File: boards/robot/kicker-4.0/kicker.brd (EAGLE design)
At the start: 141 x 146.1 mm, 158 parts, among them J1 B2PS-VH(LF)(SN), J100 B2PS-VH(LF)(SN), J101 B2PS-VH(LF)(SN), J2 2-PIN_2MM-H, J3 3-PIN_2MM-H, J4 SFW8R-1STE1LF, Q1 BSS127, Q100 AOD1N60, Q101 BSS127, Q2 BSS127, Q3 BSS127, Q4 BSS806NSOT-23-3, Q5 ATP302ATPAK, Q6 IXGK400N30A3, Q7 IXGK400N30A3, Q8 IRFS4227, T1 DA203X-ALDA2034, U1 IX4427N, U100 15V, U2 MPM3620GQV-P, U3 ADUM7441CRQZ-RL7, U4 ADUM7441ARQZ-RL7, U5 AT32ATQFP44, U6 LT3751FE

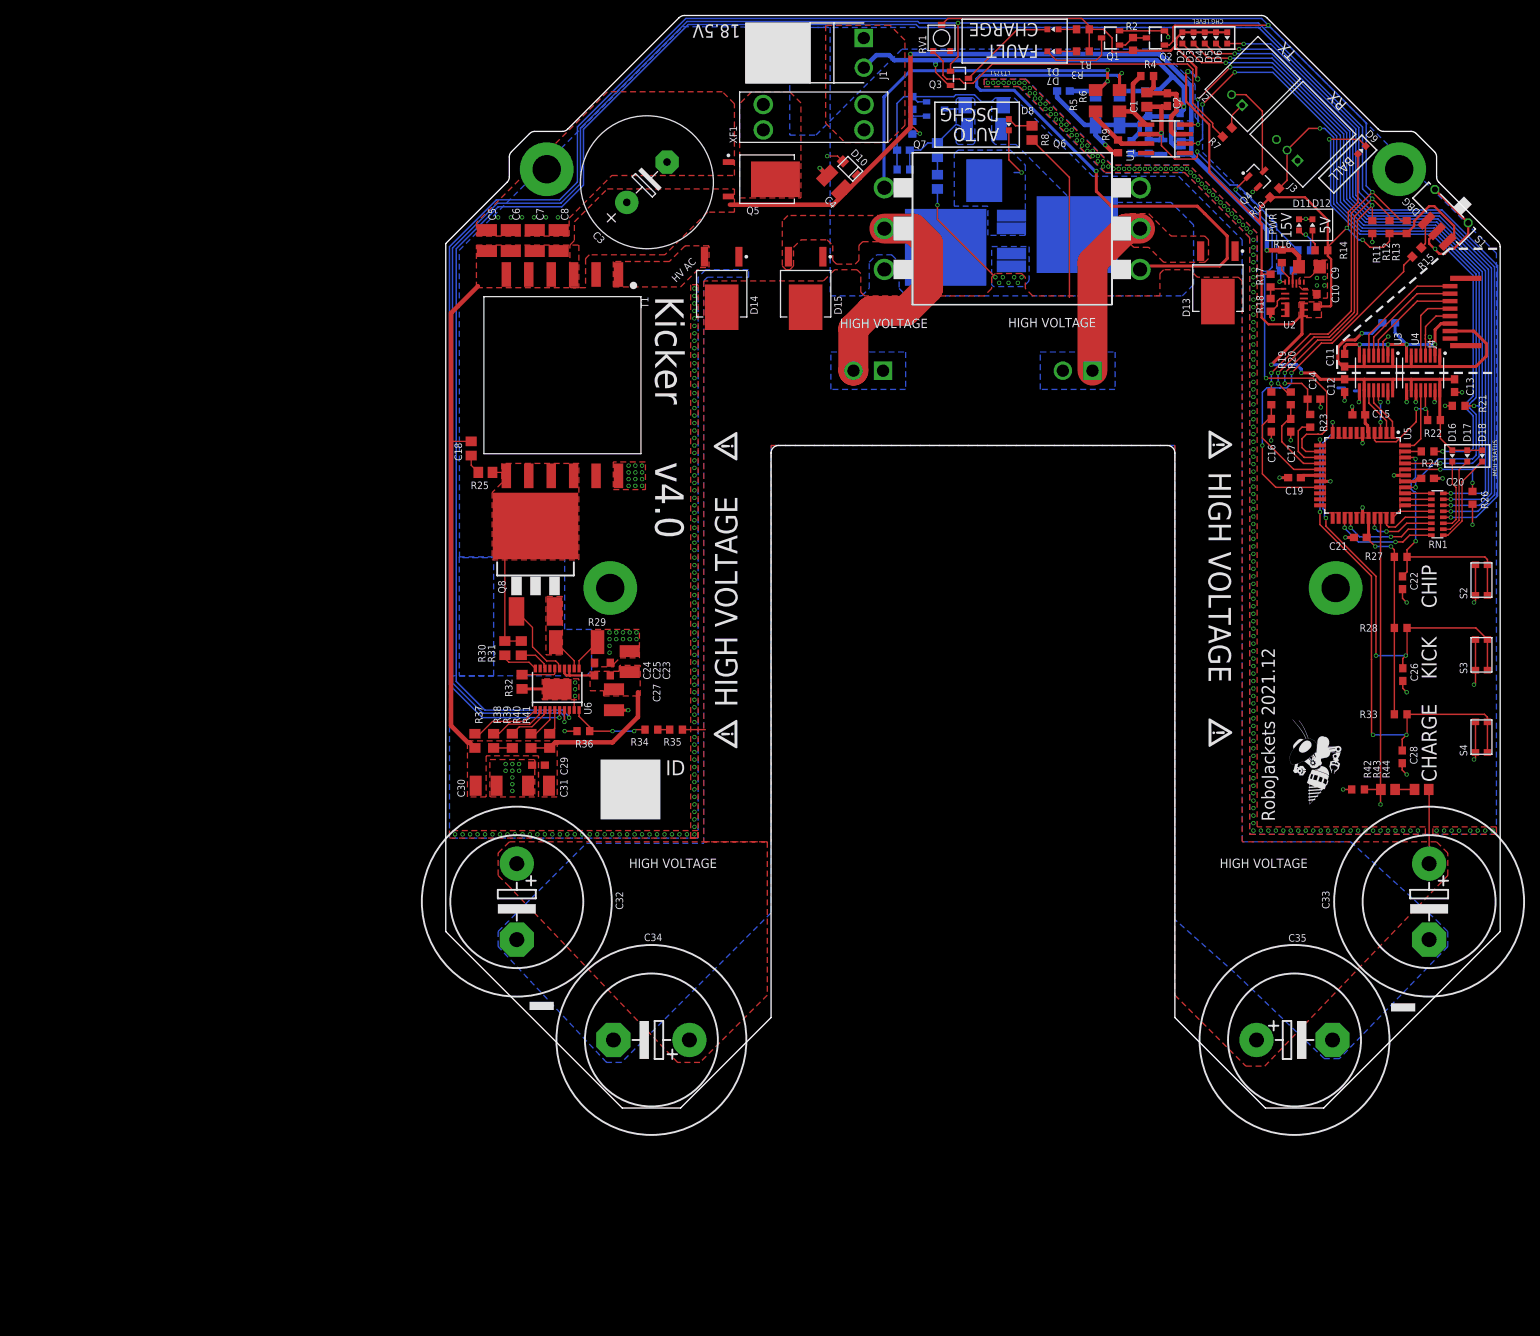
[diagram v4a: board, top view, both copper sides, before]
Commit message: Replaced power connectors
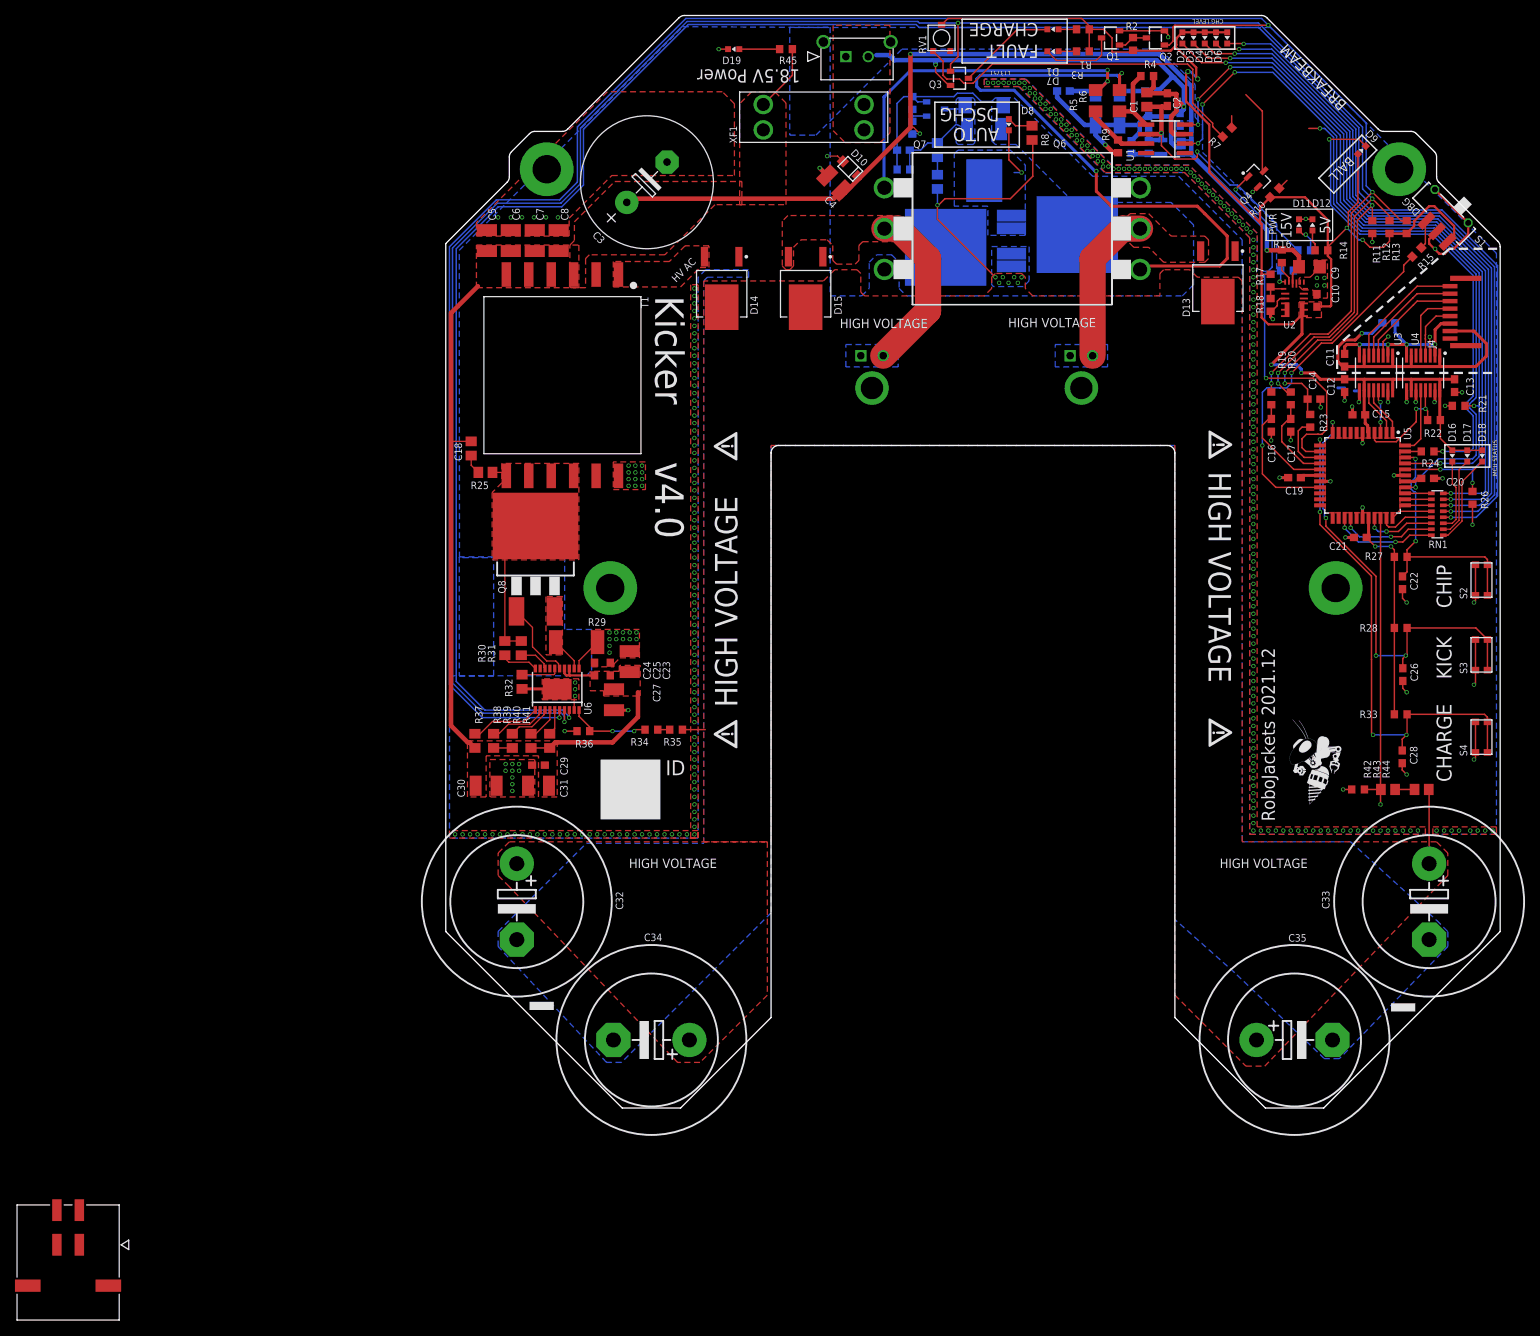
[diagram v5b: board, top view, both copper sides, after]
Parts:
- removed J1, J100, J101: B2PS-VH(LF)(SN), RoboJackets-Connectors:B2PS-CENTERED
- removed J2: 2-PIN_2MM-H, RoboJackets-Connectors:2MM-2-H
- removed J3: 3-PIN_2MM-H, RoboJackets-Connectors:2MM-3-H
- removed Q5: ATP302ATPAK, RoboJackets-Discrete:TO460P950X150-3
- added D19: GREEN, RoboJackets-LEDs:CHIP-LED0603
- added J5: 436500217, RoboJackets-Connectors:CON_436500217_MOL
- added J6, J7: 436500202, RoboJackets-Connectors:CON_436500202_MOL
- added J8: 430450411, RoboJackets-Connectors:CON_430450411_MOL
- added R45: 1k, rcl:R0603
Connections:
- removed net N$9: Q5.3, XF1.3, XF1.4
- new net 15V_PWR_BR1: D19.A, R45.1
- net BB_RX: no longer J3.2
- net BB_TX_CL: no longer J2.1
- net CHIPPER: now also J6.2; no longer J101.2
- net GND: now also D19.C, J5.1; no longer J1.2, J3.1, J3.3, Q5.1
- net KICKER: now also J7.2; no longer J100.1
- net N$19: no longer J2.2
- net N$39: now also J5.2; no longer J1.1
- net V+: now also J6.1, J7.1; no longer J100.2, J101.1
- net VBATT: now also R45.2, XF1.3, XF1.4; no longer Q5.2
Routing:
- net VBATT: track 213.7 -> 236.9 mm
- net BB_RX: track 82.0 -> 73.9 mm
- net CHIPPER: track 30.5 -> 23.0 mm
- net 15V_PWR_BR1: track 0.00 -> 5.40 mm
- net V+: track 51.2 -> 47.3 mm
- net BB_TX_CL: track 3.58 -> 1.60 mm
- net N$19: track 13.1 -> 11.2 mm
- net KICKER: track 22.7 -> 21.0 mm
- net GND: track 237.1 -> 236.1 mm, vias 375 -> 376
- removed copper zone on layer 1, net N$9
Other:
- board text added: "18.5V Power"
- board text added: "BREAKBEAM"
- board text removed: "18.5V"
- board text removed: "RX"
- board text removed: "TX"
- board text removed: "x"

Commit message: Repalced breakbeam connector
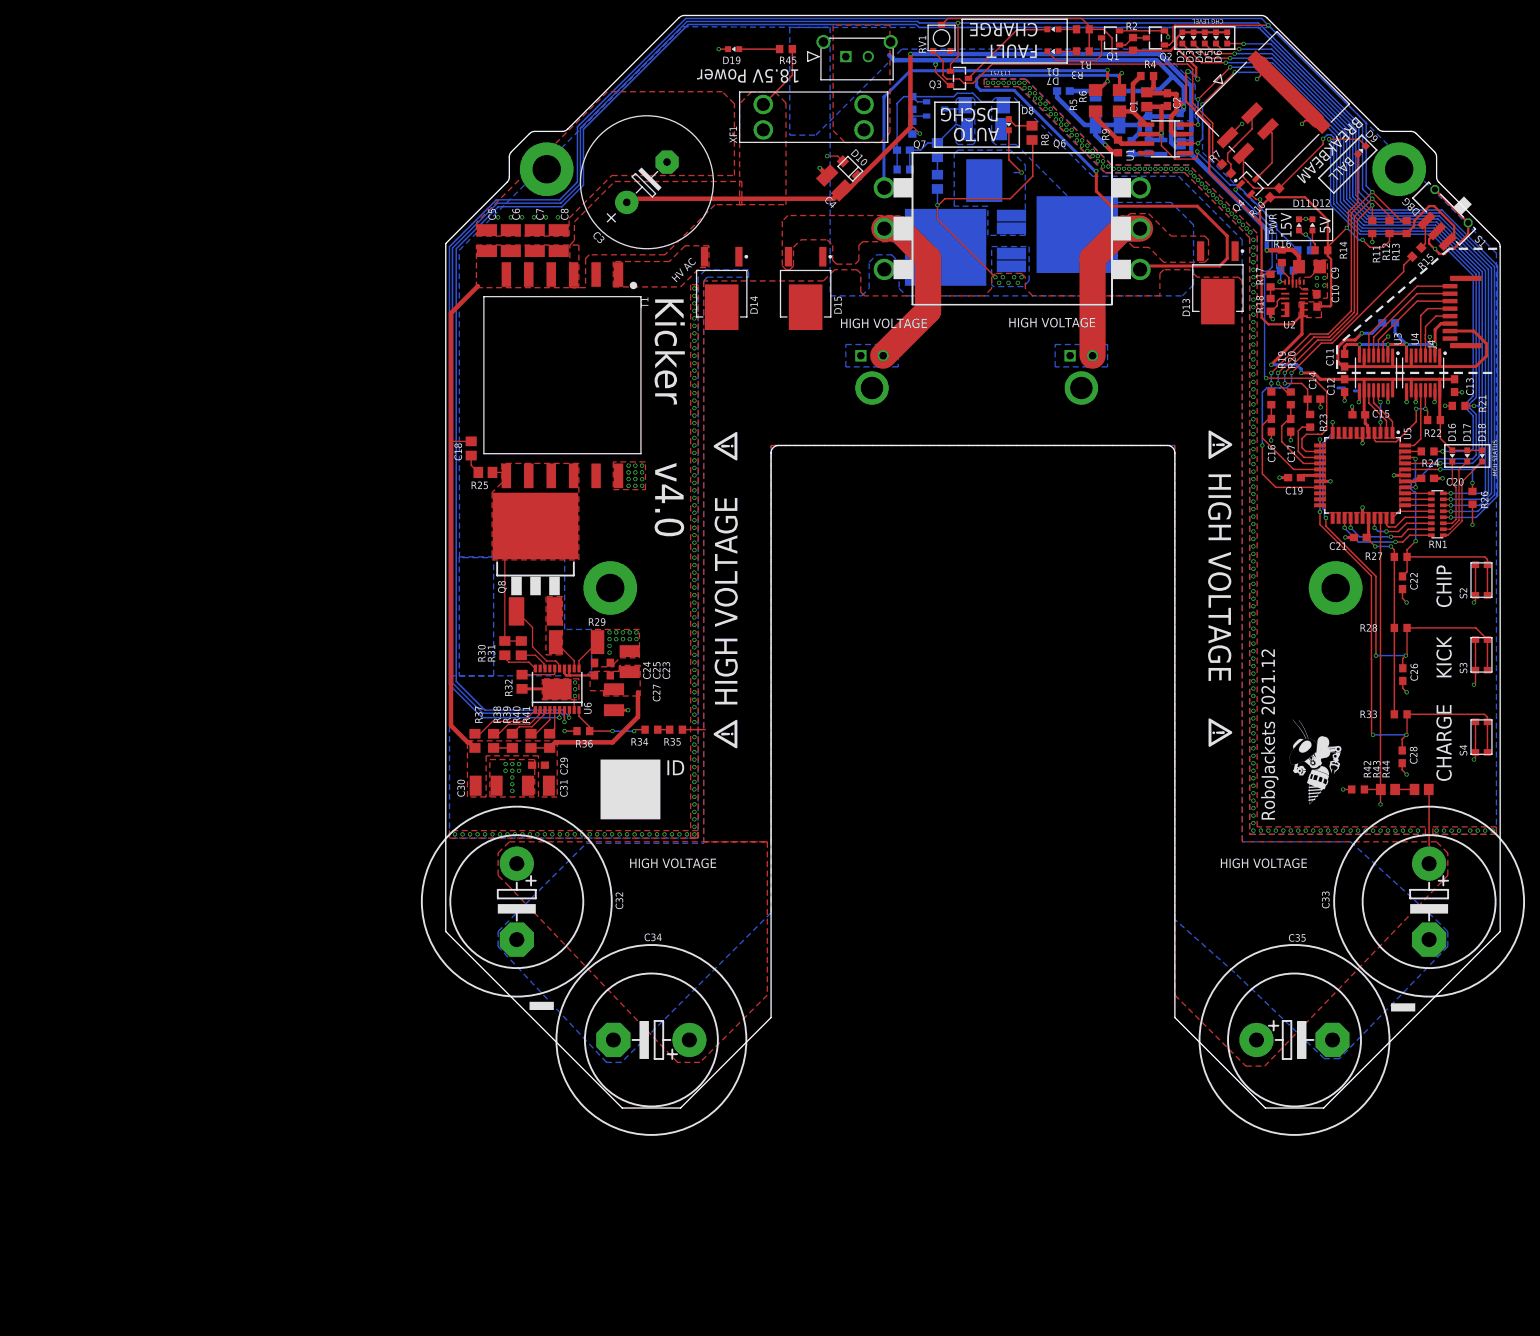
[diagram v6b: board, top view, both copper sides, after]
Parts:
- moved J8 227.7 mm to (42.0, 67.0), turned to 135 degrees
- moved R7 4.90 mm to (33.9, 57.0), turned to 315 degrees
- moved Q4 1.41 mm to (37.2, 55.0)
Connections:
- net BB_RX: now also J8.4
- net BB_TX_CL: now also J8.1
- net GND: now also J8.3, J8.S1, J8.S2
- net N$19: now also J8.2
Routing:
- net GND: track 236.1 -> 252.8 mm, vias 376 -> 379
- net BB_RX: track 73.9 -> 87.9 mm
- net BB_TX_CL: track 1.60 -> 9.58 mm
- net N$3: track 49.7 -> 53.3 mm
- net N$19: track 11.2 -> 7.69 mm
- net BB_TX: track 51.8 -> 50.4 mm
- net VBATT: track 236.9 -> 236.1 mm
